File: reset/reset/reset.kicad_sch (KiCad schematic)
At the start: 1 part

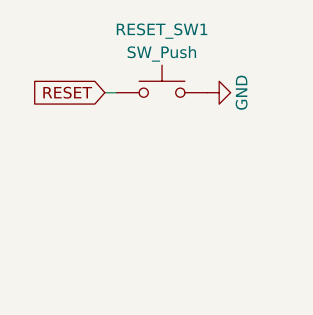
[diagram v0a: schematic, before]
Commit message: update reset, remove led
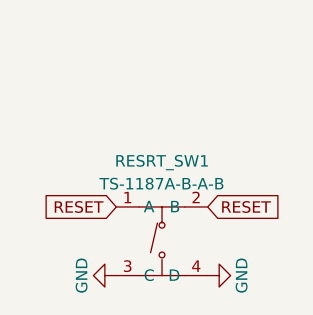
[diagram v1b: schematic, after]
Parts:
- removed RESET_SW1: SW_Push, ErgoCai.pretty:K2-1187SQ, symbol Switch:SW_Push
- added RESRT_SW1: TS-1187A-B-A-B, ErgoCai.pretty:SW-SMD_4P-L5.1-W5.1-P3.70-LS6.5-TL_H1.5, symbol ErgoCai:TS-1187A-B-A-B
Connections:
- net GND: now also RESRT_SW1.3 (C), RESRT_SW1.4 (D)
- net RESET: now also RESRT_SW1.1 (A), RESRT_SW1.2 (B)
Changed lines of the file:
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@@
 	(generator_version "9.0")
 	(paper "A4")
-	(wire
-		(pts
-			(xy 72.39 67.31) (xy 73.66 67.31)
-		)
-		(stroke
-			(width 0)
-			(type solid)
-		)
-	)
 	(global_label "RESET"
 		(shape input)
-		(at 72.39 67.31 180)
+		(at 83.82 80.01 0)
 		(fields_autoplaced yes)
 		(effects
@@
 				(size 1.27 1.27)
 			)
+			(justify left)
+		)
+		(property "Intersheetrefs" "${INTERSHEET_REFS}"
+			(at 92.5503 80.01 0)
+			(effects
+				(font
+					(size 1.27 1.27)
+				)
+				(justify left)
+				(hide yes)
+			)
+		)
+	)
+	(global_label "RESET"
+		(shape input)
+		(at 73.66 80.01 180)
+		(fields_autoplaced yes)
+		(effects
+			(font
+				(size 1.27 1.27)
+			)
 			(justify right)
 		)
 		(property "Intersheetrefs" "${INTERSHEET_REFS}"
-			(at 63.6597 67.31 0)
+			(at 64.9297 80.01 0)
 			(effects
 				(font
@@
 	(symbol
 		(lib_id "power:GND")
-		(at 83.82 67.31 90)
+		(at 83.82 87.63 90)
+		(unit 1)
+		(exclude_from_sim no)
+		(in_bom yes)
+		(on_board yes)
+		(dnp no)
+		(property "Reference" "#PWR01"
+			(at 90.17 87.63 0)
+			(effects
+				(font
+					(size 1.27 1.27)
+				)
+				(hide yes)
+			)
+		)
+		(property "Value" "GND"
+			(at 87.63 87.63 0)
+			(effects
+				(font
+					(size 1.27 1.27)
+				)
+			)
+		)
+		(property "Footprint" ""
+			(at 83.82 87.63 0)
+			(effects
+				(font
+					(size 1.27 1.27)
+				)
+				(hide yes)
+			)
+		)
+		(property "Datasheet" ""
+			(at 83.82 87.63 0)
+			(effects
+				(font
+					(size 1.27 1.27)
+				)
+				(hide yes)
+			)
+		)
+		(property "Description" "Power symbol creates a global label with name \"GND\" , ground"
+			(at 83.82 87.63 0)
+			(effects
+				(font
+					(size 1.27 1.27)
+				)
+				(hide yes)
+			)
+		)
+		(pin "1"
+		)
+		(instances
+			(project "reset"
+				(path "/bfa7eed2-3077-427f-9556-fd2cbd0f3928"
+					(reference "#PWR01")
+					(unit 1)
+				)
+			)
+		)
+	)
+	(symbol
+		(lib_id "power:GND")
+		(at 73.66 87.63 270)
 		(unit 1)
 		(exclude_from_sim no)
@@
 		(dnp no)
 		(property "Reference" "#PWR0103"
-			(at 90.17 67.31 0)
+			(at 67.31 87.63 0)
 			(effects
 				(font
@@
 		)
 		(property "Value" "GND"
-			(at 87.63 67.31 0)
+			(at 69.85 87.63 0)
 			(effects
 				(font
@@
 		)
 		(property "Footprint" ""
-			(at 83.82 67.31 0)
+			(at 73.66 87.63 0)
 			(effects
 				(font
@@
 		)
 		(property "Datasheet" ""
-			(at 83.82 67.31 0)
+			(at 73.66 87.63 0)
 			(effects
 				(font
@@
 		)
 		(property "Description" "Power symbol creates a global label with name \"GND\" , ground"
-			(at 83.82 67.31 0)
+			(at 73.66 87.63 0)
 			(effects
 				(font
@@
 	)
 	(symbol
-		(lib_id "Switch:SW_Push")
-		(at 78.74 67.31 0)
+		(lib_id "ErgoCai:TS-1187A-B-A-B")
+		(at 78.74 82.55 0)
 		(unit 1)
 		(exclude_from_sim no)
@@
 		(on_board yes)
 		(dnp no)
-		(property "Reference" "RESET_SW1"
-			(at 78.74 60.325 0)
-			(effects
-				(font
-					(size 1.27 1.27)
-				)
-			)
-		)
-		(property "Value" "SW_Push"
-			(at 78.74 62.865 0)
-			(effects
-				(font
-					(size 1.27 1.27)
-				)
-			)
-		)
-		(property "Footprint" "ErgoCai.pretty:K2-1187SQ"
-			(at 78.74 62.23 0)
-			(effects
-				(font
-					(size 1.27 1.27)
-				)
-				(hide yes)
-			)
-		)
-		(property "Datasheet" "~"
-			(at 78.74 62.23 0)
-			(effects
-				(font
-					(size 1.27 1.27)
-				)
-				(hide yes)
-			)
-		)
-		(property "Description" "Push button switch, generic, two pins"
-			(at 78.74 67.31 0)
+		(fields_autoplaced yes)
+		(property "Reference" "RESRT_SW1"
+			(at 78.74 74.93 0)
+			(effects
+				(font
+					(size 1.27 1.27)
+				)
+			)
+		)
+		(property "Value" "TS-1187A-B-A-B"
+			(at 78.74 77.47 0)
+			(effects
+				(font
+					(size 1.27 1.27)
+				)
+			)
+		)
+		(property "Footprint" "ErgoCai.pretty:SW-SMD_4P-L5.1-W5.1-P3.70-LS6.5-TL_H1.5"
+			(at 78.74 95.25 0)
+			(effects
+				(font
+					(size 1.27 1.27)
+				)
+				(hide yes)
+			)
+		)
+		(property "Datasheet" "https://lcsc.com/product-detail/Tactile-Switches_XKB-Enterprise-TS-1187-B-A-A_C318884.html"
+			(at 78.74 97.79 0)
+			(effects
+				(font
+					(size 1.27 1.27)
+				)
+				(hide yes)
+			)
+		)
+		(property "Description" ""
+			(at 78.74 82.55 0)
+			(effects
+				(font
+					(size 1.27 1.27)
+				)
+				(hide yes)
+			)
+		)
+		(property "LCSC Part" "C318884"
+			(at 78.74 100.33 0)
 			(effects
 				(font
@@
 		(pin "2"
 		)
+		(pin "3"
+		)
+		(pin "4"
+		)
 		(instances
-			(project "reset"
+			(project ""
 				(path "/bfa7eed2-3077-427f-9556-fd2cbd0f3928"
-					(reference "RESET_SW1")
+					(reference "RESRT_SW1")
 					(unit 1)
 				)
